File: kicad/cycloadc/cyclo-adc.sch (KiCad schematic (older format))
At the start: 9 parts, among them P1 CONN_8, P2 CONN_8, U1 TL431LP

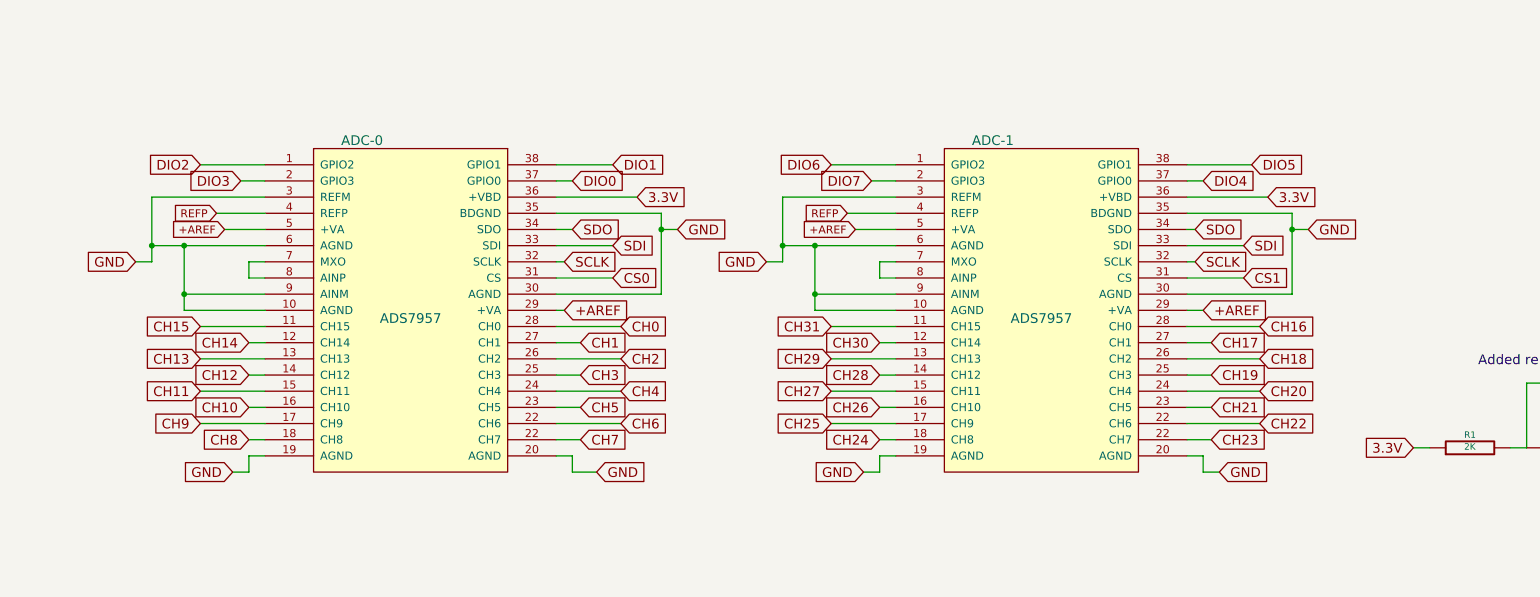
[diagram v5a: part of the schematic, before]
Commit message: redo of adc board with thicker traces, caps next to adc chips.
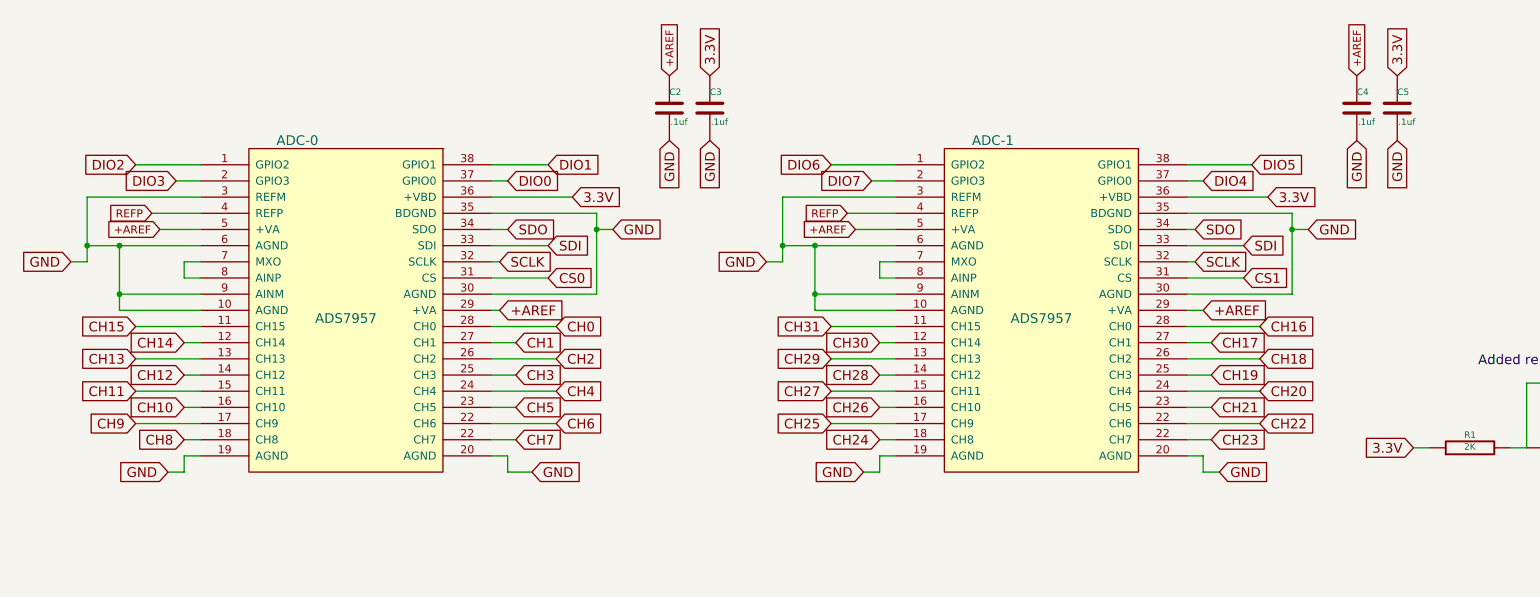
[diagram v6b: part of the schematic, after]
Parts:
- added C2, C3, C4, C5: .1uf, ~, symbol C
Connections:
- net +AREF: now also C2.1, C4.1
- net 3.3V: now also C3.1, C5.1
- net GND: now also C2.2, C3.2, C4.2, C5.2
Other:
- moved on the sheet: ADC-0
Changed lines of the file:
@@
 Text GLabel 9200 3050 2    60   Input ~ 0
 3.3V
-Text GLabel 5300 3050 2    60   Input ~ 0
+Text GLabel 4900 3050 2    60   Input ~ 0
 3.3V
-Text GLabel 9450 3250 2    60   Input ~ 0
-GND
-Text GLabel 5550 3250 2    60   Input ~ 0
-GND
-Text GLabel 2200 3450 0    60   Input ~ 0
-GND
-Text GLabel 5050 4750 2    60   Input ~ 0
-GND
-Text GLabel 2800 4750 0    60   Input ~ 0
+Text GLabel 10000 2700 3    60   Input ~ 0
+GND
+Text GLabel 5150 3250 2    60   Input ~ 0
+GND
+Text GLabel 1800 3450 0    60   Input ~ 0
+GND
+Text GLabel 4650 4750 2    60   Input ~ 0
+GND
+Text GLabel 2400 4750 0    60   Input ~ 0
 GND
 Text GLabel 8900 4750 2    60   Input ~ 0
@@
 Text GLabel 6750 2950 0    60   Input ~ 0
 DIO7
-Text GLabel 2850 2950 0    60   Input ~ 0
+Text GLabel 2450 2950 0    60   Input ~ 0
 DIO3
-Text GLabel 2600 2850 0    60   Input ~ 0
+Text GLabel 2200 2850 0    60   Input ~ 0
 DIO2
-Text GLabel 4900 2950 2    60   Input ~ 0
+Text GLabel 4500 2950 2    60   Input ~ 0
 DIO0
-Text GLabel 5150 2850 2    60   Input ~ 0
+Text GLabel 4750 2850 2    60   Input ~ 0
 DIO1
 Text GLabel 8800 7750 2    60   Input ~ 0
@@
 Text GLabel 8800 6950 2    60   Input ~ 0
 DIO3
-Text GLabel 2600 3850 0    60   Input ~ 0
+Text GLabel 2200 3850 0    60   Input ~ 0
 CH15
-Text GLabel 2900 3950 0    60   Input ~ 0
+Text GLabel 2500 3950 0    60   Input ~ 0
 CH14
-Text GLabel 2600 4050 0    60   Input ~ 0
+Text GLabel 2200 4050 0    60   Input ~ 0
 CH13
-Text GLabel 2900 4150 0    60   Input ~ 0
+Text GLabel 2500 4150 0    60   Input ~ 0
 CH12
-Text GLabel 2600 4250 0    60   Input ~ 0
+Text GLabel 2200 4250 0    60   Input ~ 0
 CH11
-Text GLabel 2900 4350 0    60   Input ~ 0
+Text GLabel 2500 4350 0    60   Input ~ 0
 CH10
-Text GLabel 2600 4450 0    60   Input ~ 0
+Text GLabel 2200 4450 0    60   Input ~ 0
 CH9
-Text GLabel 2900 4550 0    60   Input ~ 0
+Text GLabel 2500 4550 0    60   Input ~ 0
 CH8
-Text GLabel 4950 4550 2    60   Input ~ 0
+Text GLabel 4550 4550 2    60   Input ~ 0
 CH7
-Text GLabel 5200 4450 2    60   Input ~ 0
+Text GLabel 4800 4450 2    60   Input ~ 0
 CH6
-Text GLabel 4950 4350 2    60   Input ~ 0
+Text GLabel 4550 4350 2    60   Input ~ 0
 CH5
-Text GLabel 5200 4250 2    60   Input ~ 0
+Text GLabel 4800 4250 2    60   Input ~ 0
 CH4
-Text GLabel 4950 4150 2    60   Input ~ 0
+Text GLabel 4550 4150 2    60   Input ~ 0
 CH3
-Text GLabel 5200 4050 2    60   Input ~ 0
+Text GLabel 4800 4050 2    60   Input ~ 0
 CH2
-Text GLabel 4950 3950 2    60   Input ~ 0
+Text GLabel 4550 3950 2    60   Input ~ 0
 CH1
-Text GLabel 5200 3850 2    60   Input ~ 0
+Text GLabel 4800 3850 2    60   Input ~ 0
 CH0
-Text GLabel 5150 3550 2    60   Input ~ 0
+Text GLabel 4750 3550 2    60   Input ~ 0
 CS0
-Text GLabel 4850 3450 2    60   Input ~ 0
+Text GLabel 4450 3450 2    60   Input ~ 0
 SCLK
-Text GLabel 5150 3350 2    60   Input ~ 0
+Text GLabel 4750 3350 2    60   Input ~ 0
 SDI
-Text GLabel 4900 3250 2    60   Input ~ 0
+Text GLabel 4500 3250 2    60   Input ~ 0
 SDO
-Text GLabel 4850 3750 2    60   Input ~ 0
+Text GLabel 4450 3750 2    60   Input ~ 0
 +AREF
 Text GLabel 14500 3750 0    60   Input ~ 0
@@
 	6800 3450 6900 3450
 Wire Wire Line
-	5450 3150 5450 3650
-Wire Wire Line
-	5450 3650 4800 3650
+	5050 3150 5050 3650
+Wire Wire Line
+	5050 3650 4400 3650
 Wire Wire Line
 	6200 3450 6100 3450
 Wire Wire Line
-	5050 4750 4900 4750
+	4650 4750 4500 4750
 Wire Wire Line
 	6800 4750 6800 4650
@@
 	6800 4750 6700 4750
 Wire Wire Line
-	3000 2850 2600 2850
+	2600 2850 2200 2850
 Wire Wire Line
 	6900 2850 6500 2850
@@
 	8350 7750 8800 7750
 Wire Wire Line
-	4950 4550 4800 4550
+	4550 4550 4400 4550
 Wire Wire Line
 	8700 4550 8850 4550
 Wire Wire Line
-	3000 4450 2600 4450
-Wire Wire Line
-	3000 4250 2600 4250
-Wire Wire Line
-	2600 4050 3000 4050
-Wire Wire Line
-	2600 3850 3000 3850
-Wire Wire Line
-	4950 4350 4800 4350
-Wire Wire Line
-	4950 4150 4800 4150
-Wire Wire Line
-	4950 3950 4800 3950
-Wire Wire Line
-	4800 4650 4900 4650
-Connection ~ 2500 3650
-Wire Wire Line
-	2500 3350 2500 3750
-Wire Wire Line
-	2500 3750 3000 3750
-Wire Wire Line
-	4800 3550 5150 3550
-Wire Wire Line
-	4800 3350 5150 3350
-Wire Wire Line
-	3000 3550 2900 3550
-Wire Wire Line
-	2900 3550 2900 3450
-Wire Wire Line
-	2900 3450 3000 3450
-Wire Wire Line
-	5450 3150 4800 3150
-Wire Wire Line
-	2900 4650 2900 4750
-Wire Wire Line
-	4900 4650 4900 4750
-Wire Wire Line
-	2300 3350 3000 3350
-Wire Wire Line
-	4800 3750 4850 3750
-Wire Wire Line
-	5300 3050 4800 3050
-Wire Wire Line
-	3000 3050 2300 3050
-Wire Wire Line
-	2300 3050 2300 3450
-Connection ~ 2300 3350
-Wire Wire Line
-	4850 3450 4800 3450
-Wire Wire Line
-	3000 3650 2500 3650
-Connection ~ 2500 3350
-Wire Wire Line
-	2900 4650 3000 4650
-Wire Wire Line
-	5200 3850 4800 3850
-Wire Wire Line
-	5200 4050 4800 4050
-Wire Wire Line
-	5200 4250 4800 4250
-Wire Wire Line
-	5200 4450 4800 4450
-Wire Wire Line
-	3000 3950 2900 3950
-Wire Wire Line
-	2900 4150 3000 4150
-Wire Wire Line
-	3000 4350 2900 4350
-Wire Wire Line
-	3000 4550 2900 4550
-Wire Wire Line
-	4800 2950 4900 2950
-Wire Wire Line
-	2850 2950 3000 2950
+	2600 4450 2200 4450
+Wire Wire Line
+	2600 4250 2200 4250
+Wire Wire Line
+	2200 4050 2600 4050
+Wire Wire Line
+	2200 3850 2600 3850
+Wire Wire Line
+	4550 4350 4400 4350
+Wire Wire Line
+	4550 4150 4400 4150
+Wire Wire Line
+	4550 3950 4400 3950
+Wire Wire Line
+	4400 4650 4500 4650
+Connection ~ 2100 3650
+Wire Wire Line
+	2100 3350 2100 3750
+Wire Wire Line
+	2100 3750 2600 3750
+Wire Wire Line
+	4400 3550 4750 3550
+Wire Wire Line
+	4400 3350 4750 3350
+Wire Wire Line
+	2600 3550 2500 3550
+Wire Wire Line
+	2500 3550 2500 3450
+Wire Wire Line
+	2500 3450 2600 3450
+Wire Wire Line
+	5050 3150 4400 3150
+Wire Wire Line
+	2500 4650 2500 4750
+Wire Wire Line
+	4500 4650 4500 4750
+Wire Wire Line
+	1900 3350 2600 3350
+Wire Wire Line
+	4400 3750 4450 3750
+Wire Wire Line
+	4900 3050 4400 3050
+Wire Wire Line
+	2600 3050 1900 3050
+Wire Wire Line
+	1900 3050 1900 3450
+Connection ~ 1900 3350
+Wire Wire Line
+	4450 3450 4400 3450
+Wire Wire Line
+	2600 3650 2100 3650
+Connection ~ 2100 3350
+Wire Wire Line
+	2500 4650 2600 4650
+Wire Wire Line
+	4800 3850 4400 3850
+Wire Wire Line
+	4800 4050 4400 4050
+Wire Wire Line
+	4800 4250 4400 4250
+Wire Wire Line
+	4800 4450 4400 4450
+Wire Wire Line
+	2600 3950 2500 3950
+Wire Wire Line
+	2500 4150 2600 4150
+Wire Wire Line
+	2600 4350 2500 4350
+Wire Wire Line
+	2600 4550 2500 4550
+Wire Wire Line
+	4400 2950 4500 2950
+Wire Wire Line
+	2450 2950 2600 2950
 Wire Wire Line
 	6750 2950 6900 2950
@@
 	9100 2850 8700 2850
 Wire Wire Line
-	4800 2850 5150 2850
+	4400 2850 4750 2850
 Wire Wire Line
 	14650 4350 14550 4350
@@
 	8800 4750 8900 4750
 Wire Wire Line
-	2900 4750 2800 4750
-Wire Wire Line
-	2300 3450 2200 3450
-Wire Wire Line
-	5450 3250 5550 3250
-Connection ~ 5450 3250
+	2500 4750 2400 4750
+Wire Wire Line
+	1900 3450 1800 3450
+Wire Wire Line
+	5050 3250 5150 3250
+Connection ~ 5050 3250
 Connection ~ 9350 3250
 Wire Wire Line
@@
 	9350 3150 9350 3650
 Wire Wire Line
-	4900 3250 4800 3250
+	4500 3250 4400 3250
 Wire Wire Line
 	8350 8650 9100 8650
@@
 Wire Wire Line
 	6600 3150 6900 3150
-Text GLabel 2750 3250 0    49   Input ~ 0
+Text GLabel 2350 3250 0    49   Input ~ 0
 +AREF
 Wire Wire Line
-	2750 3250 3000 3250
-Text GLabel 2700 3150 0    49   Input ~ 0
+	2350 3250 2600 3250
+Text GLabel 2300 3150 0    49   Input ~ 0
 REFP
 Wire Wire Line
-	2700 3150 3000 3150
+	2300 3150 2600 3150
 Text GLabel 14600 3950 0    60   Input ~ 0
 SDO
@@
 L ADS7957 ADC-0
 U 1 1 535ECE01
-P 3900 3900
-F 0 "ADC-0" H 3600 5100 60  0000 C CNN
-F 1 "ADS7957" H 3900 4000 60  0000 C CNN
-F 2 "" H 3900 3900 60  0000 C CNN
-F 3 "" H 3900 3900 60  0000 C CNN
-	1    3900 3900
+P 3500 3900
+F 0 "ADC-0" H 3200 5100 60  0000 C CNN
+F 1 "ADS7957" H 3500 4000 60  0000 C CNN
+F 2 "" H 3500 3900 60  0000 C CNN
+F 3 "" H 3500 3900 60  0000 C CNN
+	1    3500 3900
 	1    0    0    -1
 $EndComp
@@
 Text GLabel 12000 4700 3    60   Input ~ 0
 GND
+$Comp
+L C C5
+U 1 1 53608756
+P 10000 2500
+F 0 "C5" H 10000 2600 40  0000 L CNN
+F 1 ".1uf" H 10006 2415 40  0000 L CNN
+F 2 "~" H 10038 2350 30  0000 C CNN
+F 3 "~" H 10000 2500 60  0000 C CNN
+	1    10000 2500
+	1    0    0    -1
+$EndComp
+Text GLabel 10000 2300 1    60   Input ~ 0
+3.3V
+Text GLabel 9750 2700 3    60   Input ~ 0
+GND
+$Comp
+L C C4
+U 1 1 53608984
+P 9750 2500
+F 0 "C4" H 9750 2600 40  0000 L CNN
+F 1 ".1uf" H 9756 2415 40  0000 L CNN
+F 2 "~" H 9788 2350 30  0000 C CNN
+F 3 "~" H 9750 2500 60  0000 C CNN
+	1    9750 2500
+	1    0    0    -1
+$EndComp
+Text GLabel 9750 2300 1    49   Input ~ 0
++AREF
+Text GLabel 5750 2700 3    60   Input ~ 0
+GND
+$Comp
+L C C3
+U 1 1 53608BFD
+P 5750 2500
+F 0 "C3" H 5750 2600 40  0000 L CNN
+F 1 ".1uf" H 5756 2415 40  0000 L CNN
+F 2 "~" H 5788 2350 30  0000 C CNN
+F 3 "~" H 5750 2500 60  0000 C CNN
+	1    5750 2500
+	1    0    0    -1
+$EndComp
+Text GLabel 5750 2300 1    60   Input ~ 0
+3.3V
+Text GLabel 5500 2700 3    60   Input ~ 0
+GND
+$Comp
+L C C2
+U 1 1 53608C05
+P 5500 2500
+F 0 "C2" H 5500 2600 40  0000 L CNN
+F 1 ".1uf" H 5506 2415 40  0000 L CNN
+F 2 "~" H 5538 2350 30  0000 C CNN
+F 3 "~" H 5500 2500 60  0000 C CNN
+	1    5500 2500
+	1    0    0    -1
+$EndComp
+Text GLabel 5500 2300 1    49   Input ~ 0
++AREF
+Text GLabel 9450 3250 2    60   Input ~ 0
+GND
 $EndSCHEMATC
